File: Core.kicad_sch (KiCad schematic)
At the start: 5 parts, among them J25 Conn_01x05_Pin, J26 2-2013289-1, U7 M24C02-WMN

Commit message: updated schematic
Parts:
- removed J26: 2-2013289-1, xbot_core:xbot_core, symbol local_SODIMM:2-2013289-1
- added J26: xcore, xcore:xcore, symbol xcore:xcore
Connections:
- net 3.3V_Out: now also J26.19 (3.3V_Output), J26.21 (3.3V_Output)
- net 5V_IN: now also J26.1 (5V_Input), J26.11 (5V_Input), J26.13 (5V_Input), J26.15 (5V_Input), J26.17 (5V_Input), J26.3 (5V_Input), J26.5 (5V_Input), J26.7 (5V_Input), J26.9 (5V_Input)
- net AGPIO0: now also J26.149 (AGPIO0)
- net AGPIO1: now also J26.151 (AGPIO1)
- net AGPIO2: now also J26.153 (AGPIO2)
- net AGPIO3: now also J26.155 (AGPIO3)
- net AGPIO4: now also J26.157 (AGPIO4)
- net AGPIO5: now also J26.159 (AGPIO5)
- net CM_FAN_PWM: now also J26.164 (CM_FAN_PWM)
- net ETH0.LED_G: now also J26.70 (ETH0.LED_Green)
- net ETH0.LED_Y: now also J26.69 (ETH0.LED_Yellow)
- net ETH0.PAIR_A_N: now also J26.63 (ETH0.Pair_A-)
- net ETH0.PAIR_A_P: now also J26.65 (ETH0.Pair_A+)
- net ETH0.PAIR_B_N: now also J26.64 (ETH0.Pair_B-)
- net ETH0.PAIR_B_P: now also J26.66 (ETH0.Pair_B+)
- net ETH0.PAIR_C_N: now also J26.57 (ETH0.Pair_C-)
- net ETH0.PAIR_C_P: now also J26.59 (ETH0.Pair_C+)
- net ETH0.PAIR_D_N: now also J26.58 (ETH0.Pair_D-)
- net ETH0.PAIR_D_P: now also J26.60 (ETH0.Pair_D+)
- net ETH1.LED_G: now also J26.54 (ETH1.LED_Green)
- net ETH1.LED_Y: now also J26.53 (ETH1.LED_Yellow)
- net ETH1.PAIR_A_N: now also J26.47 (ETH1.Pair_A-)
- net ETH1.PAIR_A_P: now also J26.49 (ETH1.Pair_A+)
- net ETH1.PAIR_B_N: now also J26.48 (ETH1.Pair_B-)
- net ETH1.PAIR_B_P: now also J26.50 (ETH1.Pair_B+)
- net ETH1.PAIR_C_N: now also J26.41 (ETH1.Pair_C-)
- net ETH1.PAIR_C_P: now also J26.43 (ETH1.Pair_C+)
- net ETH1.PAIR_D_N: now also J26.42 (ETH1.Pair_D-)
- net ETH1.PAIR_D_P: now also J26.44 (ETH1.Pair_D+)
- net ETH2.LED_G: now also J26.38 (ETH2.LED_Green)
- net ETH2.LED_Y: now also J26.37 (ETH2.LED_Yellow)
- net ETH2.PAIR_A_N: now also J26.31 (ETH2.Pair_A-)
- net ETH2.PAIR_A_P: now also J26.33 (ETH2.Pair_A+)
- net ETH2.PAIR_B_N: now also J26.32 (ETH2.Pair_B-)
- net ETH2.PAIR_B_P: now also J26.34 (ETH2.Pair_B+)
- net ETH2.PAIR_C_N: now also J26.25 (ETH2.Pair_C-)
- net ETH2.PAIR_C_P: now also J26.27 (ETH2.Pair_C+)
- net ETH2.PAIR_D_N: now also J26.26 (ETH2.Pair_D-)
- net ETH2.PAIR_D_P: now also J26.28 (ETH2.Pair_D+)
- net FDCAN1.RX: now also J26.118 (FDCAN.RX)
- net FDCAN1.TX: now also J26.116 (FDCAN.TX)
- net GND: now also J26.10 (GND), J26.104 (GND), J26.114 (GND), J26.12 (GND), J26.120 (GND), J26.14 (GND), J26.147 (GND), J26.16 (GND), J26.168 (GND), J26.173 (GND), J26.174 (GND), J26.179 (GND), J26.18 (GND), J26.180 (GND), J26.185 (GND), J26.186 (GND), J26.191 (GND), J26.192 (GND), J26.197 (GND), J26.198 (GND), J26.2 (GND), J26.203 (GND), J26.204 (GND), J26.23 (GND), J26.24 (GND), J26.29 (GND), J26.30 (GND), J26.35 (GND), J26.36 (GND), J26.39 (GND), J26.4 (GND), J26.40 (GND), J26.45 (GND), J26.46 (GND), J26.51 (GND), J26.52 (GND), J26.55 (GND), J26.56 (GND), J26.6 (GND), J26.61 (GND), J26.62 (GND), J26.67 (GND), J26.68 (GND), J26.71 (GND), J26.72 (GND), J26.73 (GND), J26.74 (GND), J26.8 (GND), J26.82 (GND), J26.87 (GND), J26.90 (GND), J26.SH1 (GND), J26.SH2 (GND)
- net GPIO0: now also J26.145 (GPIO0)
- net GPIO1: now also J26.131 (GPIO1)
- net GPIO10: now also J26.148 (GPIO10)
- net GPIO11: now also J26.146 (GPIO11)
- net GPIO12: now also J26.144 (GPIO12)
- net GPIO13: now also J26.142 (GPIO13)
- net GPIO14: now also J26.140 (GPIO14)
- net GPIO15: now also J26.138 (GPIO15)
- net GPIO16: now also J26.136 (GPIO16)
- net GPIO17: now also J26.134 (GPIO17)
- net GPIO18: now also J26.132 (GPIO18)
- net GPIO19: now also J26.130 (GPIO19)
- net GPIO2: now also J26.141 (GPIO2)
- net GPIO20: now also J26.128 (GPIO20)
- net GPIO21: now also J26.122 (GPIO21)
- net GPIO22: now also J26.124 (GPIO22)
- net GPIO23: now also J26.126 (GPIO23)
- net GPIO3: now also J26.139 (GPIO3)
- net GPIO4: now also J26.137 (GPIO4)
- net GPIO5: now also J26.133 (GPIO5)
- net GPIO6: now also J26.135 (GPIO6)
- net GPIO7: now also J26.143 (GPIO7)
- net GPIO8: now also J26.129 (GPIO8)
- net GPIO9: now also J26.127 (GPIO9)
- net I2C1.SCL: now also J26.94 (I2C1.SCL)
- net I2C1.SDA: now also J26.92 (I2C1.SDA)
- net I2C2.SCL: now also J26.98 (I2C2.SCL)
- net I2C2.SDA: now also J26.96 (I2C2.SDA)
- net I2C4_ID.SCL: now also J26.102 (ID_I2C.SCL)
- net I2C4_ID.SDA: now also J26.100 (ID_I2C.SDA)
- net I2S6.CK: now also J26.112 (I2S6.CK)
- net I2S6.SDI: now also J26.106 (I2S6.SDI)
- net I2S6.SDO: now also J26.108 (I2S6.SDO)
- net I2S6.WS: now also J26.110 (I26.WS)
- net SPI1.MISO: now also J26.76 (SPI1.MISO)
- net SPI1.MOSI: now also J26.78 (SPI1.MOSI)
- net SPI1.SCK: now also J26.80 (SPI1.SCK)
- net SPI2.MISO: now also J26.84 (SPI2.MISO)
- net SPI2.MOSI: now also J26.86 (SPI2.MOSI)
- net SPI2.SCK: now also J26.88 (SPI2.SCK)
- net STM_SWCLK: now also J26.160 (SWCLK)
- net STM_SWDIO: now also J26.162 (SWDIO)
- net UART1.RX: now also J26.81 (UART1.RX)
- net UART1.TX: now also J26.79 (UART1.TX)
- net UART10.RX: now also J26.103 (UART10.RX)
- net UART10.TX: now also J26.101 (UART10.TX)
- net UART2.RX: now also J26.91 (UART2.RX)
- net UART2.TX: now also J26.89 (UART2.TX)
- net UART4.RX: now also J26.85 (UART4.RX)
- net UART4.TX: now also J26.83 (UART4.TX)
- net UART6.RX: now also J26.77 (UART6.RX)
- net UART6.TX: now also J26.75 (UART6.TX)
- net UART7.RX: now also J26.95 (UART7.RX)
- net UART7.TX: now also J26.93 (UART7.TX)
- net UART8.RX: now also J26.99 (UART8.RX)
- net UART8.TX: now also J26.97 (UART8.TX)
- net USBH1.N: now also J26.177 (USB0_D-)
- net USBH1.P: now also J26.175 (USB0_D+)
- net USBH2.N: now also J26.183 (USB1_D-)
- net USBH2.P: now also J26.181 (USB1_D+)
- net USBH3.N: now also J26.189 (USB2_D-)
- net USBH3.P: now also J26.187 (USB2_D+)
- net USBH4.N: now also J26.195 (USB3_D-)
- net USBH4.P: now also J26.193 (USB3_D+)
- no-connect marks 26 -> 0

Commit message: Updated xcore library
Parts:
- J26: footprint xcore:xcore -> local_SODIMM:2_2013289_1
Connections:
- no-connect marks 0 -> 1
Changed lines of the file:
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@@
 		(color 0 0 0 0)
 	)
+	(no_connect
+		(at 69.85 53.34)
+	)
 	(bus_entry
 		(at 233.68 168.91)
@@
 	(wire
 		(pts
-			(xy 57.15 62.23) (xy 69.85 62.23)
+			(xy 57.15 67.31) (xy 69.85 67.31)
 		)
 		(stroke
@@
 	(wire
 		(pts
-			(xy 57.15 59.69) (xy 69.85 59.69)
+			(xy 57.15 64.77) (xy 69.85 64.77)
 		)
 		(stroke
@@
 	)
 	(label "I2C4_ID.SCL"
-		(at 57.15 62.23 0)
+		(at 57.15 67.31 0)
 		(fields_autoplaced yes)
 		(effects
@@
 	)
 	(label "I2C4_ID.SDA"
-		(at 57.15 59.69 0)
+		(at 57.15 64.77 0)
 		(fields_autoplaced yes)
 		(effects
@@
 	(hierarchical_label "STM_SWDIO"
 		(shape bidirectional)
-		(at 69.85 68.58 180)
+		(at 69.85 73.66 180)
 		(fields_autoplaced yes)
 		(effects
@@
 	(hierarchical_label "CM_FAN_PWM"
 		(shape output)
-		(at 69.85 76.2 180)
+		(at 69.85 81.28 180)
 		(fields_autoplaced yes)
 		(effects
@@
 	(hierarchical_label "STM_SWCLK"
 		(shape input)
-		(at 69.85 71.12 180)
+		(at 69.85 76.2 180)
 		(fields_autoplaced yes)
 		(effects
@@
 	)
 	(symbol
+		(lib_name "xcore_1")
 		(lib_id "xcore:xcore")
 		(at 88.9 60.96 0)
@@
 			)
 		)
-		(property "Footprint" "xcore:xcore"
+		(property "Footprint" "local_SODIMM:2_2013289_1"
 			(at 88.138 91.694 0)
 			(effects
@@
 	(symbol
 		(lib_id "power:GND")
-		(at 69.85 53.34 270)
+		(at 69.85 55.88 270)
 		(unit 1)
 		(exclude_from_sim no)
@@
 		(dnp no)
 		(property "Reference" "#PWR076"
-			(at 63.5 53.34 0)
+			(at 63.5 55.88 0)
 			(effects
 				(font
@@
 		)
 		(property "Value" "GND"
-			(at 66.04 53.3399 90)
+			(at 66.04 55.8799 90)
 			(effects
 				(font
@@
 		)
 		(property "Footprint" ""
-			(at 69.85 53.34 0)
+			(at 69.85 55.88 0)
 			(effects
 				(font
@@
 		)
 		(property "Datasheet" ""
-			(at 69.85 53.34 0)
+			(at 69.85 55.88 0)
 			(effects
 				(font
@@
 		)
 		(property "Description" "Power symbol creates a global label with name \"GND\" , ground"
-			(at 69.85 53.34 0)
+			(at 69.85 55.88 0)
 			(effects
 				(font

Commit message: Added power switch for F9P
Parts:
- J26: footprint local_SODIMM:2_2013289_1 -> xcore:xcore
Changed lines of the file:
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@@
 			)
 		)
-		(property "Footprint" "local_SODIMM:2_2013289_1"
+		(property "Footprint" "xcore:xcore"
 			(at 88.138 91.694 0)
 			(effects

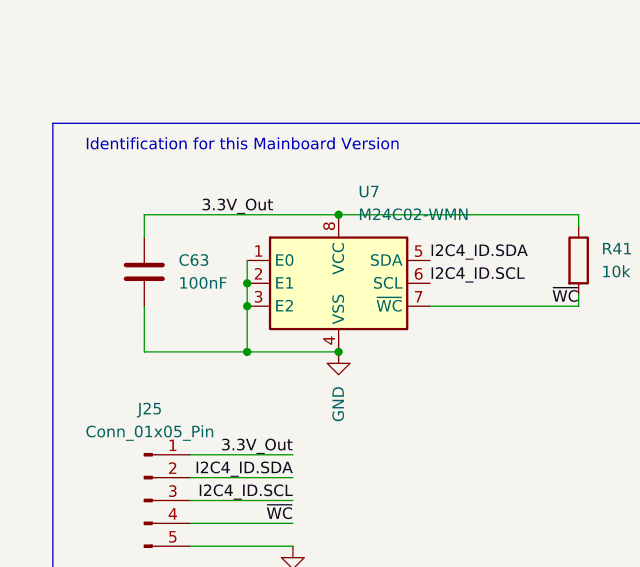
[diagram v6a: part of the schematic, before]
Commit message: Fix BOM and switch C0402 to C0603
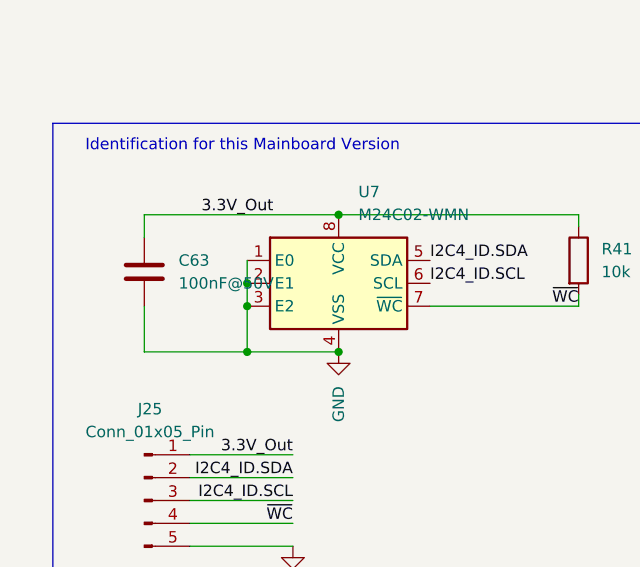
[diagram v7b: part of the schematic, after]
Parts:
- C63: value 100nF -> 100nF@50V; footprint Capacitor_SMD:C_0402_1005Metric -> Capacitor_SMD:C_0603_1608Metric; JLC C307331 -> C14663
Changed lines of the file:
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@@
 			)
 		)
-		(property "Value" "100nF"
+		(property "Value" "100nF@50V"
 			(at 27.94 245.1099 0)
 			(effects
@@
 			)
 		)
-		(property "Footprint" "Capacitor_SMD:C_0402_1005Metric"
+		(property "Footprint" "Capacitor_SMD:C_0603_1608Metric"
 			(at 25.0952 247.65 0)
 			(effects
@@
 			)
 		)
-		(property "JLC" "C307331"
+		(property "JLC" "C14663"
 			(at 24.13 243.84 0)
 			(effects

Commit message: Switch R0402 to 0603
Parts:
- R41: footprint Resistor_SMD:R_0402_1005Metric -> Resistor_SMD:R_0603_1608Metric; JLC C25744 -> C25804
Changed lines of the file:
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@@
 			)
 		)
-		(property "Footprint" "Resistor_SMD:R_0402_1005Metric"
+		(property "Footprint" "Resistor_SMD:R_0603_1608Metric"
 			(at 70.612 242.57 90)
 			(effects
@@
 			)
 		)
-		(property "JLC" "C25744"
+		(property "JLC" "C25804"
 			(at 72.39 242.57 0)
 			(effects
